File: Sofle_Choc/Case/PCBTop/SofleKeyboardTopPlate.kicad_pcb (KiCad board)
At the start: 2 copper layers, 143.4 x 111.8 mm, 34 parts, among them SW2 KEY_SWITCH

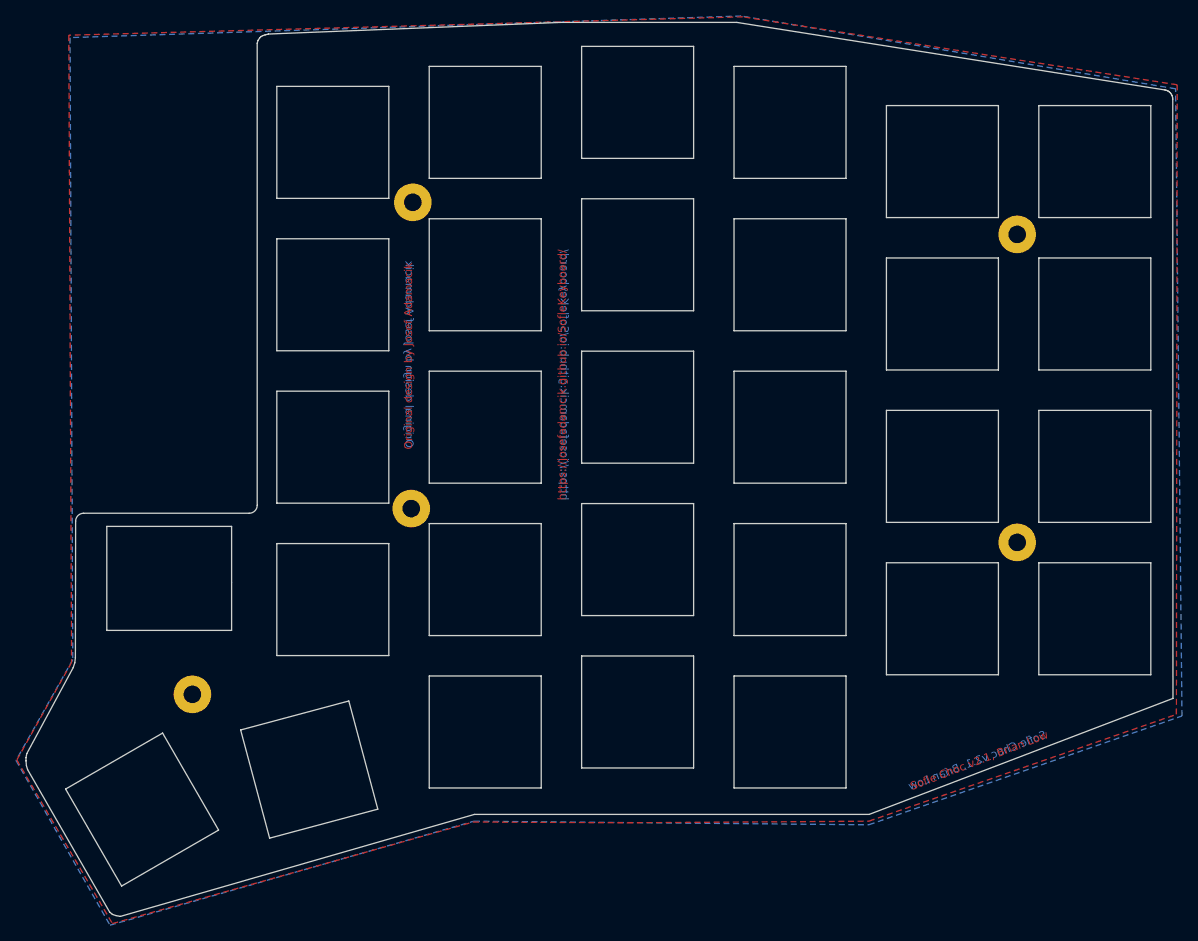
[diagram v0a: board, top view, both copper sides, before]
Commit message: Remove links from copper layer
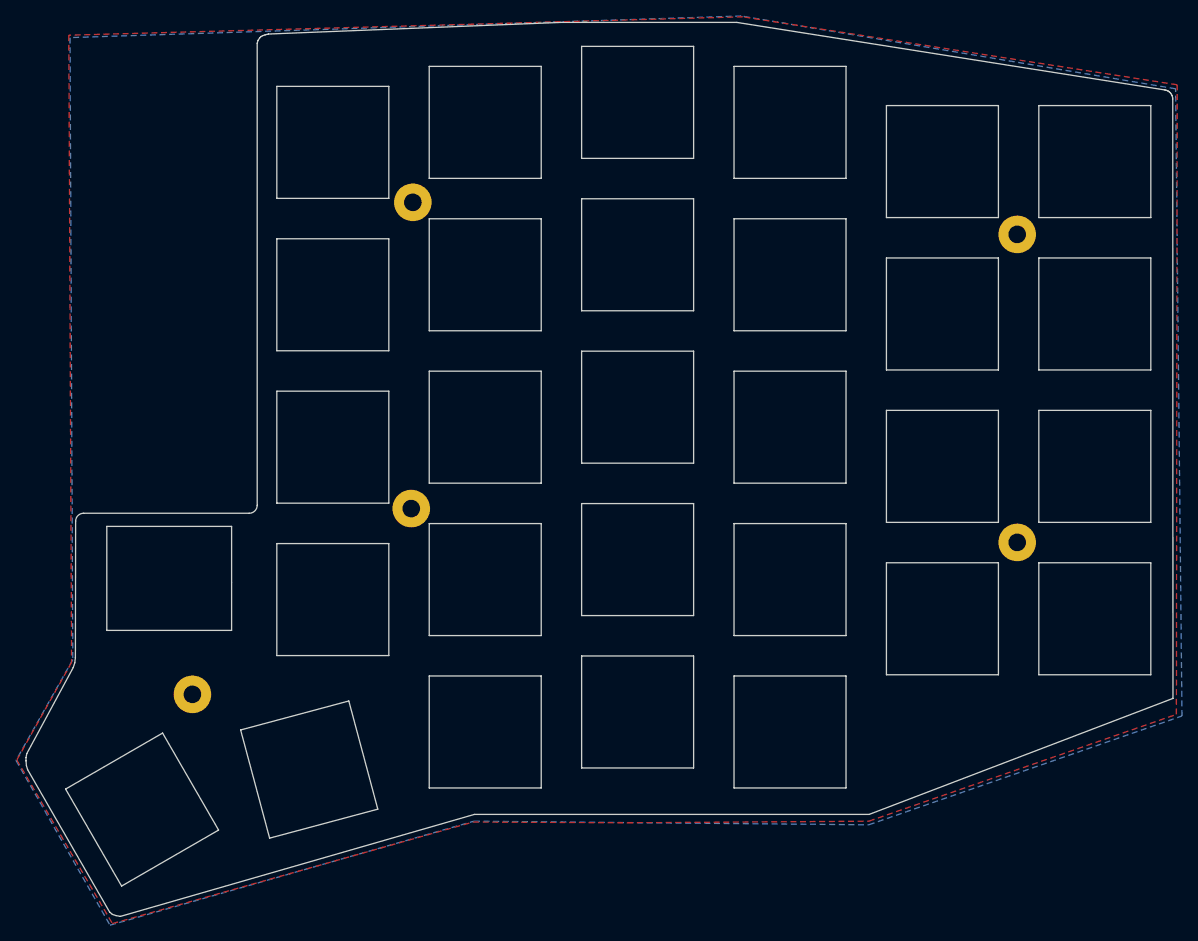
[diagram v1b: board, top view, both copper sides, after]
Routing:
- net (no net): track 0.00 -> 0.76 mm
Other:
- board text removed: "Original design by Josef Adamacik"
- board text removed: "Sofle Choc v2.1, Brian Low"
- board text removed: "https://josefadamcik.github.io/SofleKeyboard/"
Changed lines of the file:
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@@
-(kicad_pcb (version 20171130) (host pcbnew "(5.1.9-0-10_14)")
+(kicad_pcb (version 20171130) (host pcbnew "(5.1.12-1-10_14)")
   (general
     (thickness 1.6)
-    (drawings 48)
-    (tracks 0)
+    (drawings 42)
+    (tracks 3)
     (zones 0)
     (modules 34)
@@
     (pcbplotparams
       (layerselection 0x010f0_ffffffff)
-      (usegerberextensions false)
+      (usegerberextensions true)
       (usegerberattributes false)
       (usegerberadvancedattributes false)
       (creategerberjobfile false)
-      (excludeedgelayer true)
+      (excludeedgelayer false)
       (linewidth 0.100000)
       (plotframeref false)
@@
       (psa4output false)
       (plotreference true)
-      (plotvalue true)
+      (plotvalue false)
       (plotinvisibletext false)
       (padsonsilk false)
@@
       (drillshape 0)
       (scaleselection 1)
-      (outputdirectory "../../../Gerbers/Choc_v2/"))
+      (outputdirectory "../../../Gerbers/Choc_v2a/"))
   )
   (net 0 "")
@@
     (pad "" thru_hole circle (at -0.225 -0.275 90) (size 4.7 4.7) (drill 2.2) (layers *.Cu *.Mask Dwgs.User)
       (clearance 0.3))
-  )
-  (gr_text "Original design by Josef Adamacik" (at 130.895 78.1414 90) (layer F.Cu)
-    (effects (font (size 1 1) (thickness 0.2)))
-  )
-  (gr_text "Original design by Josef Adamacik" (at 130.995 77.9314 -90) (layer B.Cu)
-    (effects (font (size 1 1) (thickness 0.2)) (justify mirror))
-  )
-  (gr_text https://josefadamcik.github.io/SofleKeyboard/ (at 150.095 80.5 90) (layer F.Cu)
-    (effects (font (size 1 1) (thickness 0.15)))
-  )
-  (gr_text https://josefadamcik.github.io/SofleKeyboard/ (at 150.395 80.5 270) (layer B.Cu)
-    (effects (font (size 1 1) (thickness 0.15)) (justify mirror))
   )
   (gr_line (start 112.995 38) (end 113.395 37.9) (layer Edge.Cuts) (width 0.15))
@@
   (gr_line (start 111.995 96.8) (end 111.995 39.045) (layer Edge.Cuts) (width 0.15))
   (gr_line (start 90.3 97.8) (end 110.995 97.8) (layer Edge.Cuts) (width 0.15))
-  (gr_text "Sofle Choc v2.1, Brian Low" (at 202.245 128.695 21) (layer F.Cu)
-    (effects (font (size 1 1) (thickness 0.2)))
-  )
-  (gr_text "Sofle Choc v2.1, Brian Low" (at 201.995 128.695 21) (layer B.Cu)
-    (effects (font (size 1 1) (thickness 0.2)) (justify mirror))
-  )
   (gr_line (start 225.856871 45.026466) (end 226.021621 45.1406) (layer Edge.Cuts) (width 0.1))
   (gr_line (start 89.270257 115.845) (end 89.3 98.8) (layer Edge.Cuts) (width 0.1))
@@
   (gr_line (start 93.545 147.645) (end 83.295 129.845) (layer Edge.Cuts) (width 0.1))
   (gr_line (start 226.278881 45.442807) (end 226.365281 45.623672) (layer Edge.Cuts) (width 0.1))
+  (segment (start 131.274 58.7576) (end 131.4528 58.9364) (width 0.25) (layer B.Cu) (net 0))
+  (segment (start 131.5842 58.805) (end 131.4528 58.9364) (width 0.25) (layer B.Cu) (net 0))
+  (segment (start 207.22 101.67) (end 206.995 101.445) (width 0.25) (layer B.Cu) (net 0))
   (zone (net 0) (net_name "") (layer F.Cu) (hatch edge 0.508)
     (connect_pads (clearance 0.508))
